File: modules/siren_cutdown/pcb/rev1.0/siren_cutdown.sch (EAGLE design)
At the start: 18 parts, among them IC2 PICAXE-08M2

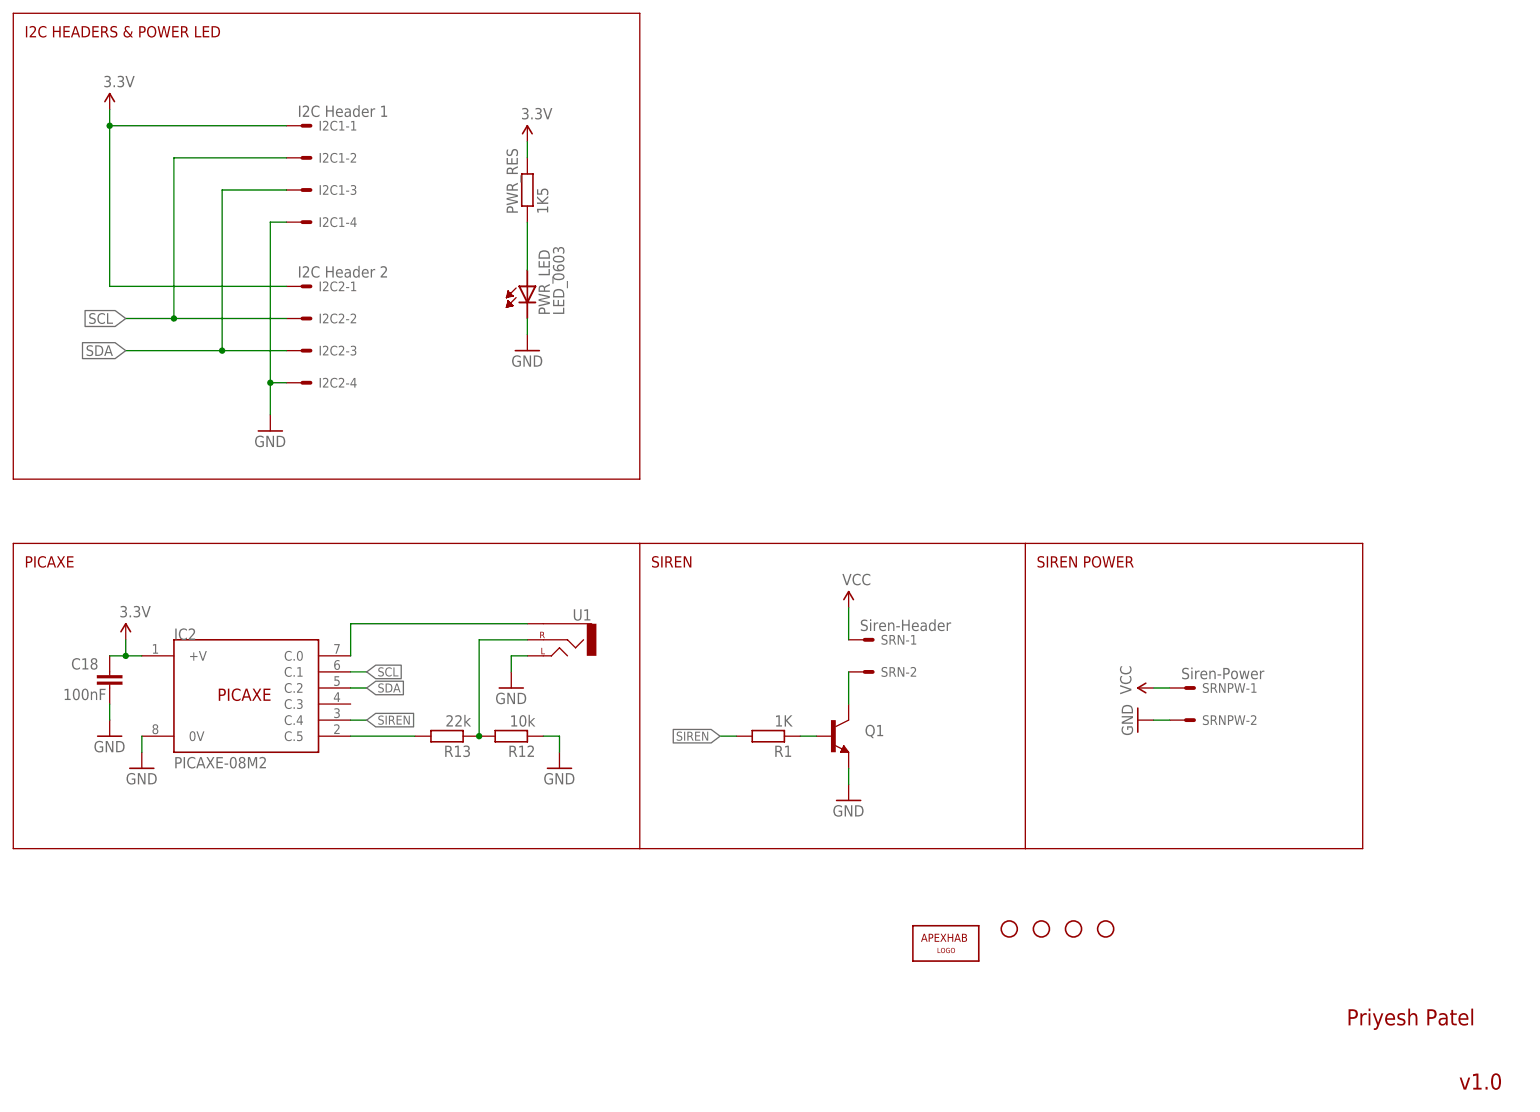
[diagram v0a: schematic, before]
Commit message: added cutdown to siren
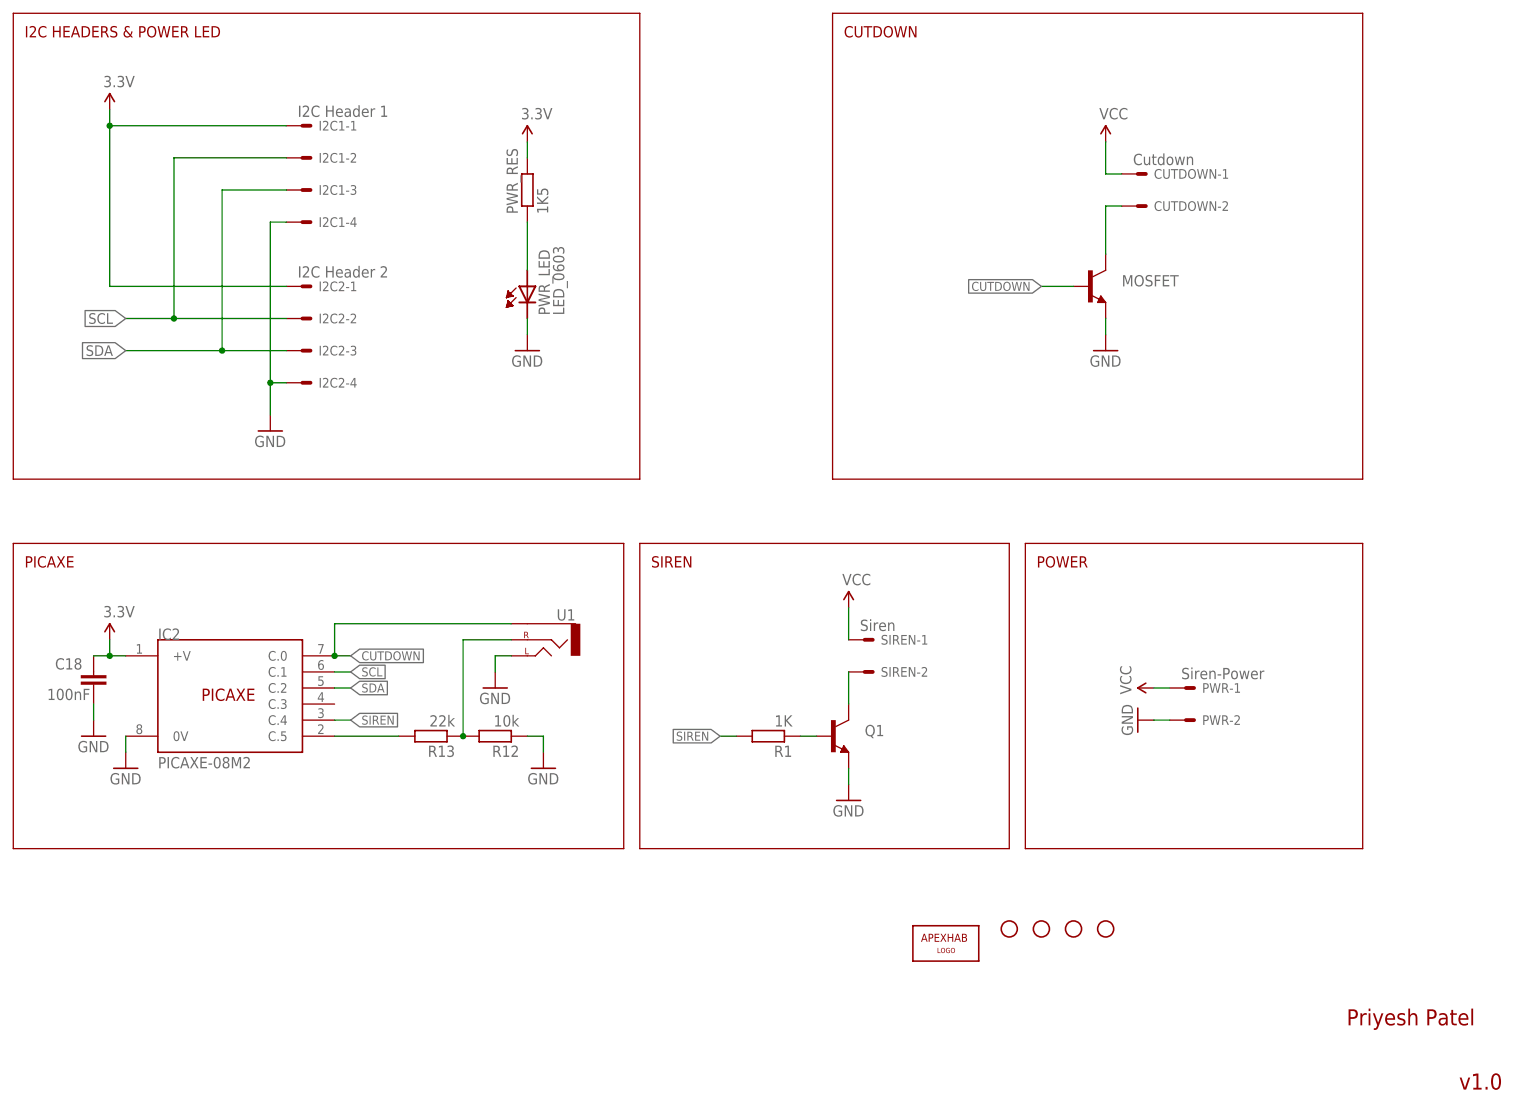
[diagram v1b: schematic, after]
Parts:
- added CUTDOWN: Cutdown, apex:22-27-2021-02
- added MOSFET: (no value), SparkFun:TRANSISTOR_NPNSOT23
- SIREN: value Siren-Header -> Siren
- renumbered SRN to SIREN, SRNPW to PWR
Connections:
- removed net N$18: IC2.C.0, U1.SLEEVE
- new net CUTDOWN: IC2.C.0, MOSFET.B, U1.SLEEVE
- new net N$4: CUTDOWN-2.S, MOSFET.C
- net GND: now also MOSFET.E
- net VCC: now also CUTDOWN-1.S
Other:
- note added: "CUTDOWN"
- note added: "POWER"
- note removed: "SIREN POWER"
- moved on the sheet: C18, IC2, R12, R13, U1
